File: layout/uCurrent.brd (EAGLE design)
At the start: 45 x 95 mm, 26 parts, among them SW1 DP3T, SW2 DP3T, U1 MAX4239ASA, U2 LMV321M5X, U3 TPS3809L30DBVR

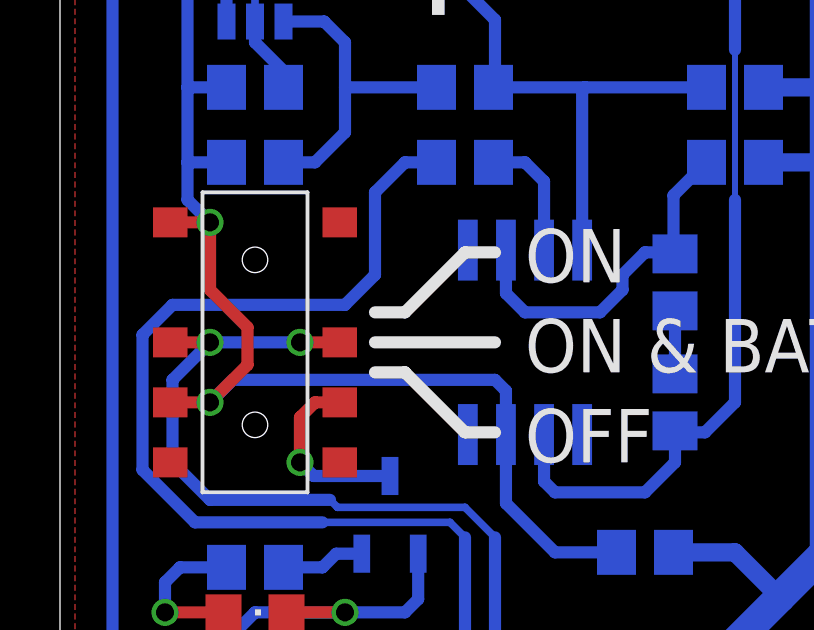
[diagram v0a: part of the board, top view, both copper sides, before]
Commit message: Forgot first Pin on OpAmp
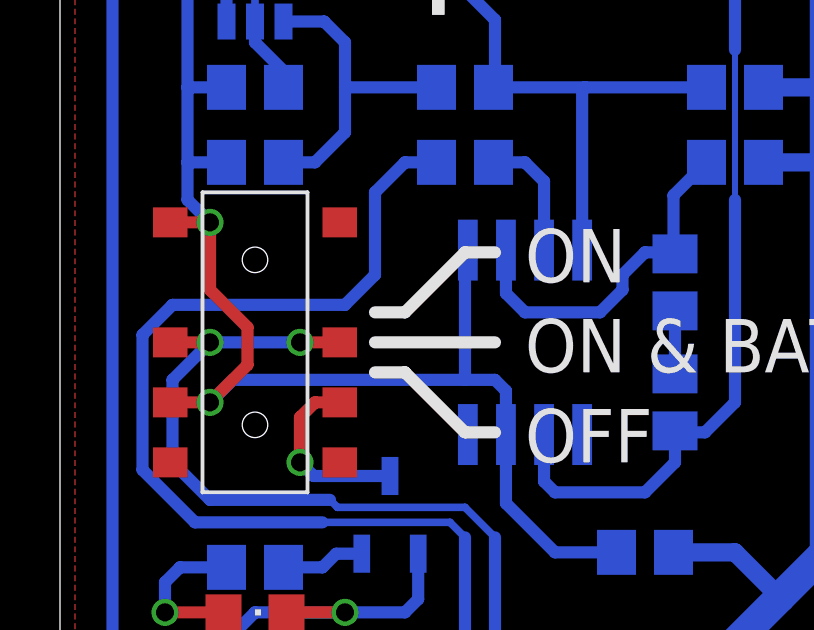
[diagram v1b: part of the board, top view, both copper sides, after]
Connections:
- net V+: now also U1.1
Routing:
- net V+: track 45.8 -> 50.2 mm
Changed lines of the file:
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@@
 <wire x1="17.365" y1="55.9266" x2="17.365" y2="57.385" width="0.4064" layer="16"/>
 <wire x1="17.365" y1="57.385" x2="17" y2="57.75" width="0.4064" layer="16"/>
-<wire x1="17" y1="57.75" x2="8.25" y2="57.75" width="0.4064" layer="16"/>
+<wire x1="17" y1="57.75" x2="16" y2="57.75" width="0.4064" layer="16"/>
+<wire x1="16" y1="57.75" x2="8.25" y2="57.75" width="0.4064" layer="16"/>
 <wire x1="8.75" y1="58.25" x2="7.5" y2="57" width="0.4064" layer="1"/>
 <via x="7.5" y="57" extent="1-16" drill="0.6"/>
@@
 <wire x1="7.5" y1="63" x2="6.75" y2="63.75" width="0.4064" layer="16"/>
 <wire x1="6.75" y1="63.75" x2="6.75" y2="65" width="0.4064" layer="16"/>
+<contactref element="U1" pad="1"/>
+<wire x1="16.095" y1="62.0734" x2="16" y2="62.0734" width="0.4064" layer="16"/>
+<wire x1="16" y1="62.0734" x2="16" y2="57.75" width="0.4064" layer="16"/>
 <wire x1="8" y1="65" x2="8.05" y2="65" width="0" layer="19" extent="16-16"/>
 </signal>
